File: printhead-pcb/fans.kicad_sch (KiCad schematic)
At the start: 13 parts, among them J14 FAN4, J4 FAN0, J5 FAN2, J7 FAN3, Q1 DTC143E, Q2 DTC143E, Q4 DTC143E, Q5 DTC143E, U2 EMC2302-2-AIZL-TR

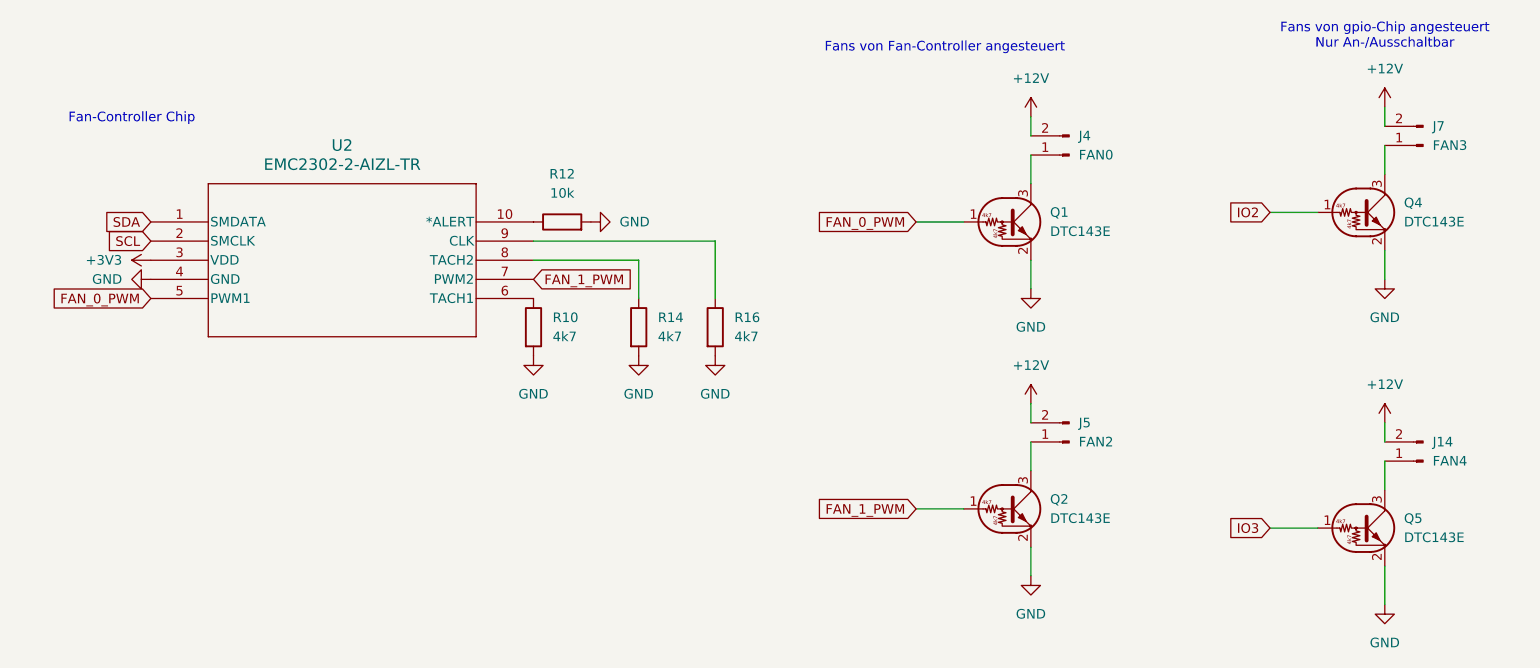
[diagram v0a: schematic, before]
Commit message: added complete list of components for i2c
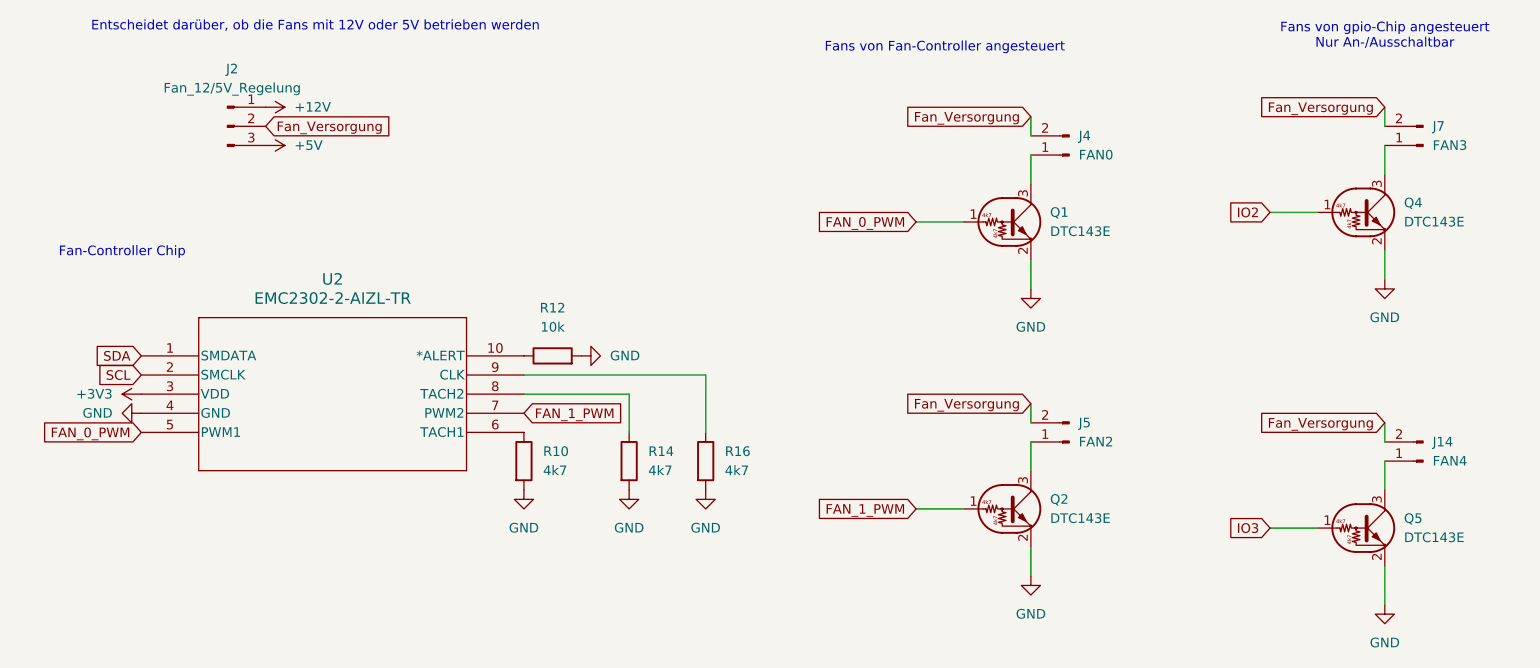
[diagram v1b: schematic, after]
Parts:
- added J2: Fan_12/5V_Regelung, symbol Connector:Conn_01x03_Pin
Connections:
- net +12V: now also J2.1 (Pin_1); no longer J14.2 (Pin_2), J4.2 (Pin_2), J5.2 (Pin_2), J7.2 (Pin_2)
- new net +5V: J2.3 (Pin_3)
- new net Fan_Versorgung: J14.2 (Pin_2), J2.2 (Pin_2), J4.2 (Pin_2), J5.2 (Pin_2), J7.2 (Pin_2)
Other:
- note added: "Entscheidet darüber, ob die Fans mit 12V oder 5V betrieben werden"
- moved on the sheet: R10, R12, R14, R16, U2

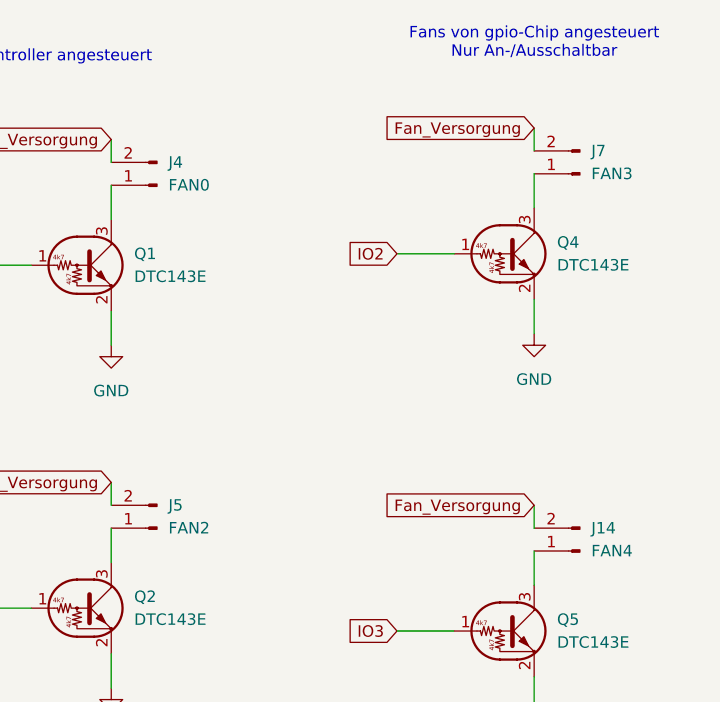
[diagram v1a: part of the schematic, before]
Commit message: implemented custom footprint
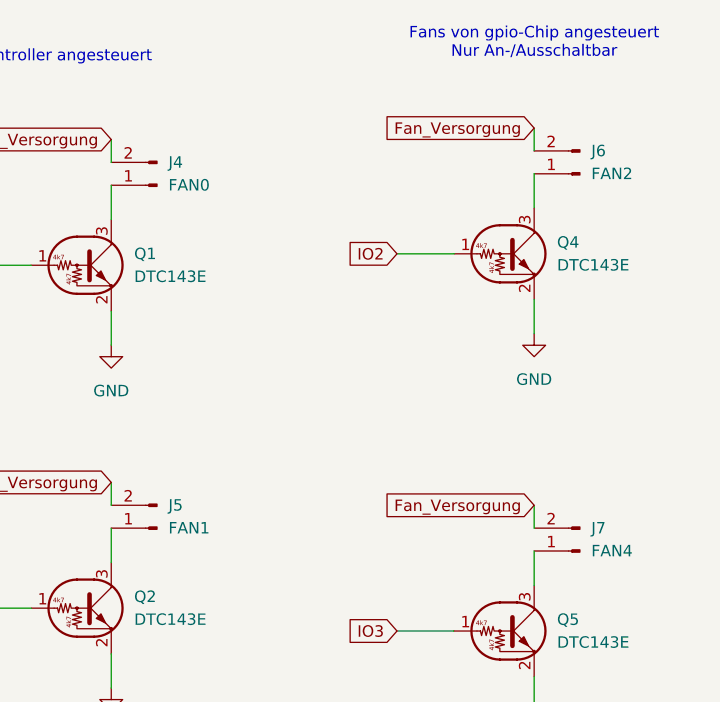
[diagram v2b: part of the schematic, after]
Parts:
- J2: footprint (none) -> Connector_PinHeader_2.54mm:PinHeader_1x03_P2.54mm_Horizontal
- J4: footprint Connector_JST:JST_EH_S2B-EH_1x02_P2.50mm_Horizontal -> Connector_PinHeader_2.54mm:PinHeader_1x02_P2.54mm_Horizontal
- J5: value FAN2 -> FAN1; footprint Connector_JST:JST_EH_B2B-EH-A_1x02_P2.50mm_Vertical -> Connector_PinHeader_2.54mm:PinHeader_1x02_P2.54mm_Horizontal
- J6: renamed from J7; value FAN3 -> FAN2; footprint Connector_JST:JST_EH_B2B-EH-A_1x02_P2.50mm_Vertical -> Connector_PinHeader_2.54mm:PinHeader_1x02_P2.54mm_Horizontal
- J7: renamed from J14; footprint Connector_JST:JST_EH_B2B-EH-A_1x02_P2.50mm_Vertical -> Connector_PinHeader_2.54mm:PinHeader_1x02_P2.54mm_Horizontal
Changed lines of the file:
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@@
 			)
 		)
-		(property "Footprint" "Connector_JST:JST_EH_S2B-EH_1x02_P2.50mm_Horizontal"
+		(property "Footprint" "Connector_PinHeader_2.54mm:PinHeader_1x02_P2.54mm_Horizontal"
 			(at 190.5 68.58 0)
 			(effects
@@
 			)
 		)
-		(property "Footprint" ""
+		(property "Footprint" "Connector_PinHeader_2.54mm:PinHeader_1x03_P2.54mm_Horizontal"
 			(at 78.74 64.77 0)
 			(effects
@@
 		(dnp no)
 		(fields_autoplaced yes)
-		(property "Reference" "J7"
+		(property "Reference" "J6"
 			(at 238.76 64.7699 0)
 			(effects
@@
 			)
 		)
-		(property "Value" "FAN3"
+		(property "Value" "FAN2"
 			(at 238.76 67.3099 0)
 			(effects
@@
 			)
 		)
-		(property "Footprint" "Connector_JST:JST_EH_B2B-EH-A_1x02_P2.50mm_Vertical"
+		(property "Footprint" "Connector_PinHeader_2.54mm:PinHeader_1x02_P2.54mm_Horizontal"
 			(at 237.49 67.31 0)
 			(effects
@@
 			(project "printhead-pcb"
 				(path "/813ad687-b864-44a5-b729-c4edf26b731d/b01a9293-0f79-4fdf-8646-1053b0e79170"
-					(reference "J7")
+					(reference "J6")
 					(unit 1)
 				)
@@
 		(dnp no)
 		(fields_autoplaced yes)
-		(property "Reference" "J14"
+		(property "Reference" "J7"
 			(at 238.76 106.6799 0)
 			(effects
@@
 			)
 		)
-		(property "Footprint" "Connector_JST:JST_EH_B2B-EH-A_1x02_P2.50mm_Vertical"
+		(property "Footprint" "Connector_PinHeader_2.54mm:PinHeader_1x02_P2.54mm_Horizontal"
 			(at 237.49 109.22 0)
 			(effects
@@
 			(project "printhead-pcb"
 				(path "/813ad687-b864-44a5-b729-c4edf26b731d/b01a9293-0f79-4fdf-8646-1053b0e79170"
-					(reference "J14")
+					(reference "J7")
 					(unit 1)
 				)
@@
 			)
 		)
-		(property "Value" "FAN2"
+		(property "Value" "FAN1"
 			(at 191.77 106.6799 0)
 			(effects
@@
 			)
 		)
-		(property "Footprint" "Connector_JST:JST_EH_B2B-EH-A_1x02_P2.50mm_Vertical"
+		(property "Footprint" "Connector_PinHeader_2.54mm:PinHeader_1x02_P2.54mm_Horizontal"
 			(at 190.5 106.68 0)
 			(effects

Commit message: second commit because autosave restored some things
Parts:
- U2: footprint EMC2302-2-AIZL-TR:MSOP10_MC_MCH -> CustomFotLibByJan:MSOP10_MC_MCH
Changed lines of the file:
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@@
 			)
 		)
-		(property "Footprint" "EMC2302-2-AIZL-TR:MSOP10_MC_MCH"
+		(property "Footprint" "CustomFotLibByJan:MSOP10_MC_MCH"
 			(at 67.31 95.25 0)
 			(effects
